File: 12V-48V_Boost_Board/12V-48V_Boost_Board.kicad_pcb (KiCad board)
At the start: 2 copper layers, 65.1 x 76.7 mm, 50 parts, among them J1 12V Input, J3 Output Current Sensing, J4 48V Output, J5 Output Measuring, J6 Output Current Sensing, Q1 FDWS86068-F085, U2 INA290A3, U3 INA290A3, U4 LP2985-5.0

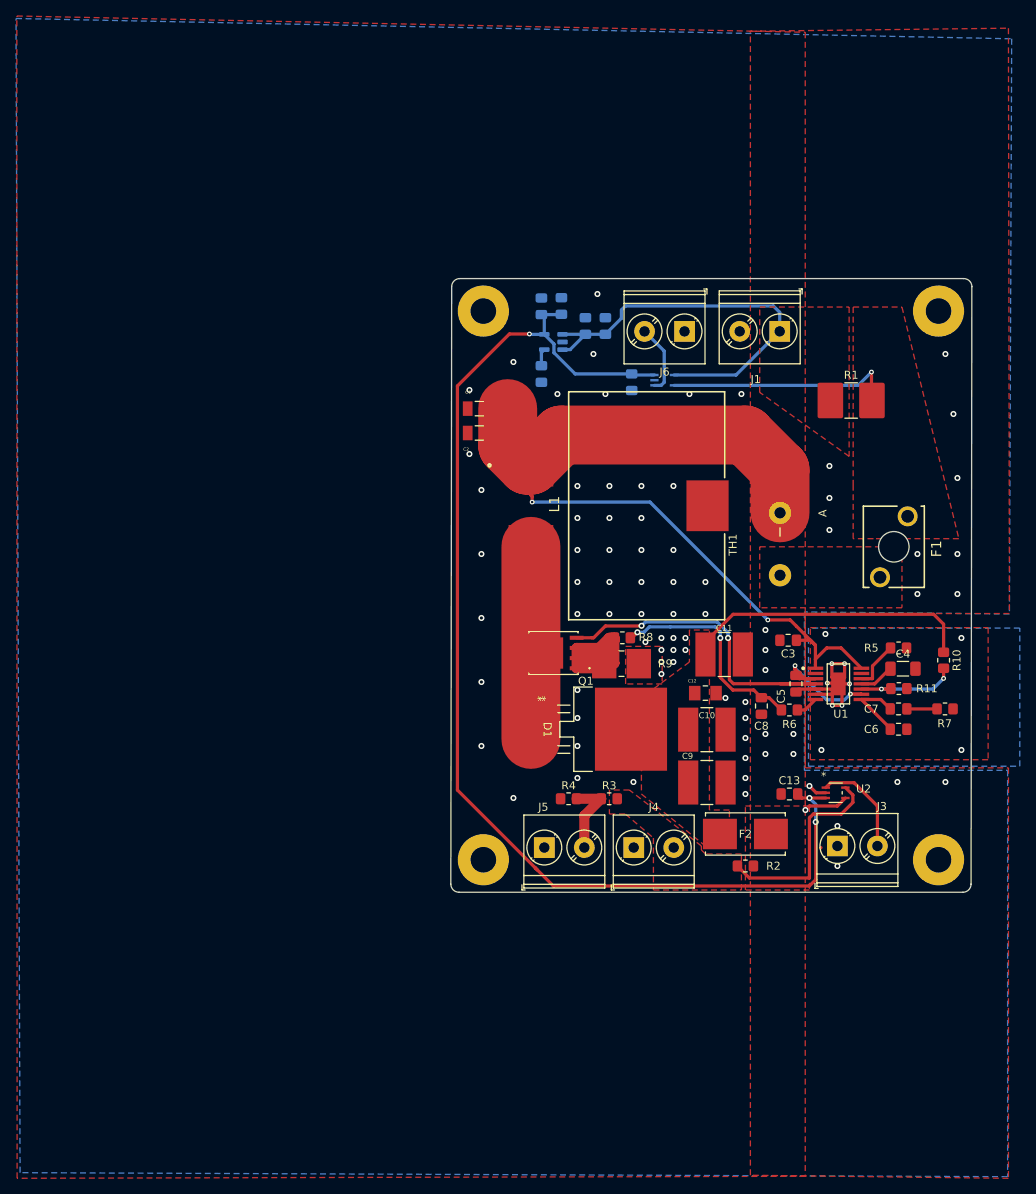
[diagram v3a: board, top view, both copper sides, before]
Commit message: PCB changes. See descp.
- Moved input current sense and 5V LDO in order not to obstruct GND return.
- Fixed silkscreen.
- Adjusted plane connections, plane sizes and thermal reliefs.

Ready for final review.
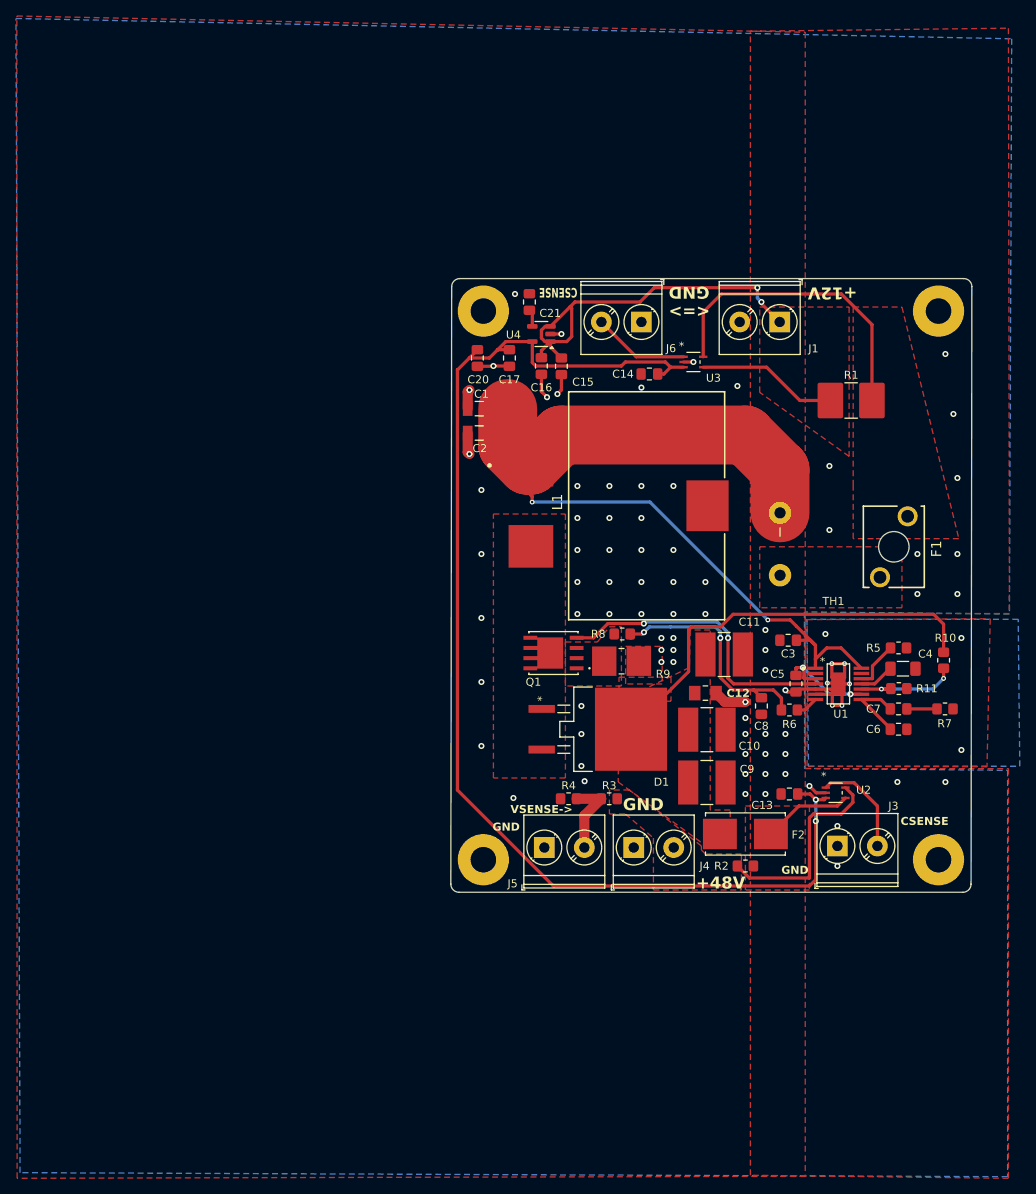
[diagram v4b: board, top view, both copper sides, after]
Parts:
- C14, C15, C16, C17, C20, C21, U3, U4: moved to F.Cu
- moved C20 10.3 mm to (110.0, 78.0), turned to -90 degrees
- moved C17 9.19 mm to (114.0, 78.0), turned to -90 degrees
- moved C21 9.12 mm to (116.5, 71.0), turned to 90 degrees
- moved C15 7.46 mm to (120.5, 79.0), turned to -90 degrees
- moved C16 7.43 mm to (118.0, 79.0), turned to -90 degrees
- moved J6 5.52 mm to (130.5, 73.5)
- moved U3 4.30 mm to (137.0, 78.5)
- moved C14 2.44 mm to (131.5, 80.0), turned to 0 degrees
- moved U4 1.80 mm to (118.0, 75.0)
- moved J1 1.17 mm to (147.8, 73.5)
- moved R8 0.47 mm to (128.1, 112.5)
- moved R9 0.30 mm to (128.0, 115.9)
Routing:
- net Net-(Q1-S): track 27.0 -> 0.00 mm
- net Net-(D1-A): track 24.1 -> 0.00 mm
- net GND: track 26.2 -> 49.2 mm, vias 90 -> 87
- net /Boost_Board_Chip/48V_OUTPUT: track 42.2 -> 59.1 mm
- net +12V: track 51.1 -> 66.4 mm, vias 0 -> 2
- net /IN-: track 29.0 -> 38.8 mm, vias 1 -> 0
- net Net-(U2-IN+): track 5.62 -> 11.2 mm, vias 1 -> 0
- net /Boost_Board_Chip/DITHOFF: track 17.9 -> 13.3 mm
- net +5V: track 150.4 -> 154.8 mm, vias 3 -> 2
- net Net-(Q1-G): track 41.6 -> 37.2 mm
- net Net-(J6-Pin_2): track 8.77 -> 12.1 mm
- net Net-(C8-Pad1): track 27.1 -> 29.4 mm
- added copper zone on F.Cu, net Net-(D1-A)
- added copper zone on F.Cu, net Net-(Q1-S)
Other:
- board text added: "*"
- board text added: "+12V"
- board text added: "+48V"
- board text added: "<=> GND"
- board text added: "CSENSE"
- board text added: "GND"
- board text added: "VSENSE"
- board text added: "VSENSE->"

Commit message: Moved current sense amps. Other minor changes.
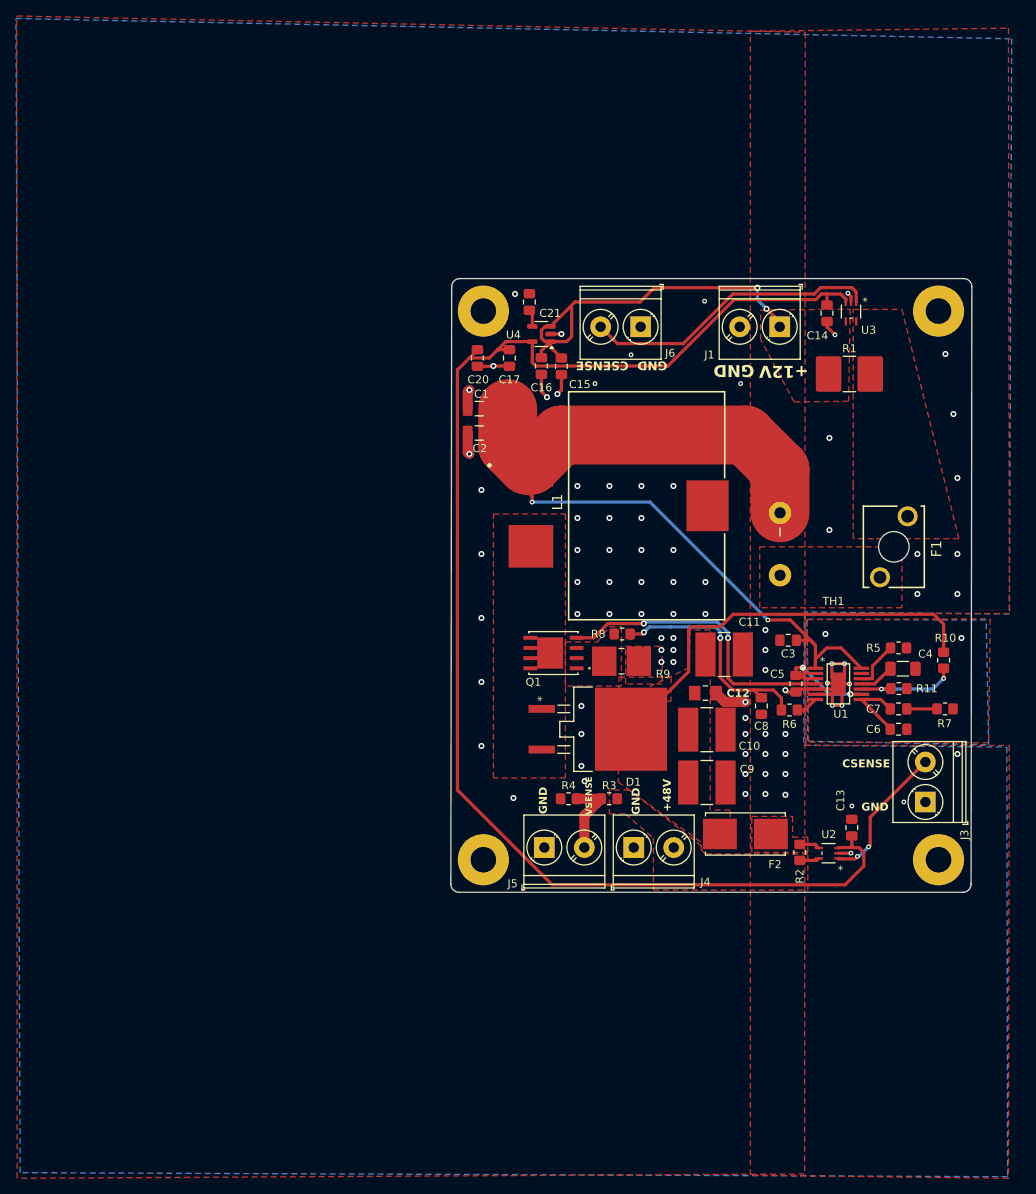
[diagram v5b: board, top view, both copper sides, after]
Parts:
- moved C14 23.5 mm to (153.7, 72.4), turned to 90 degrees
- moved U3 20.7 mm to (156.7, 72.2), turned to -90 degrees
- moved J3 12.3 mm to (166.0, 133.5), turned to 90 degrees
- moved C13 8.86 mm to (156.8, 136.7), turned to -90 degrees
- moved U2 7.60 mm to (153.9, 139.9), turned to 180 degrees
- moved R2 7.01 mm to (150.3, 139.8), turned to -90 degrees
- moved R1 3.32 mm to (156.5, 80.0)
- moved J6 0.61 mm to (130.4, 74.1)
- moved J1 0.60 mm to (147.8, 74.1)
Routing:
- net /IN-: track 38.8 -> 0.00 mm
- net Net-(J6-Pin_2): track 12.1 -> 37.2 mm
- net Net-(J4-Pin_2): track 25.9 -> 2.81 mm
- net +5V: track 154.8 -> 177.4 mm, vias 2 -> 0
- net +12V: track 66.4 -> 48.8 mm
- net Net-(U2-IN+): track 11.2 -> 2.56 mm
- net Net-(J3-Pin_2): track 12.9 -> 18.0 mm, vias 0 -> 2
- net GND: track 49.2 -> 50.5 mm, vias 87 -> 89
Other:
- board text removed: "<=> GND"
- board text removed: "VSENSE->"
